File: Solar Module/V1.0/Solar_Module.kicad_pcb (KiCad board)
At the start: 2 copper layers, 4 parts, among them U1 MT3608, U2 TP4057

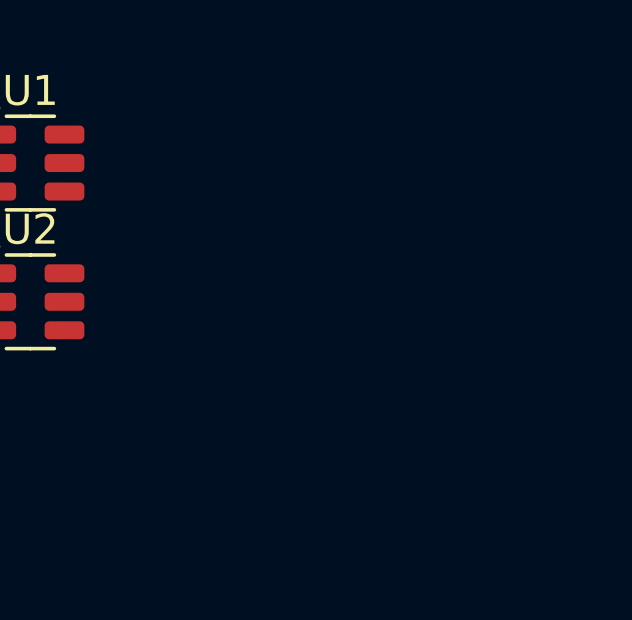
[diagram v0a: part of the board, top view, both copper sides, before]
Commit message: Added USB-C connector to schematic.
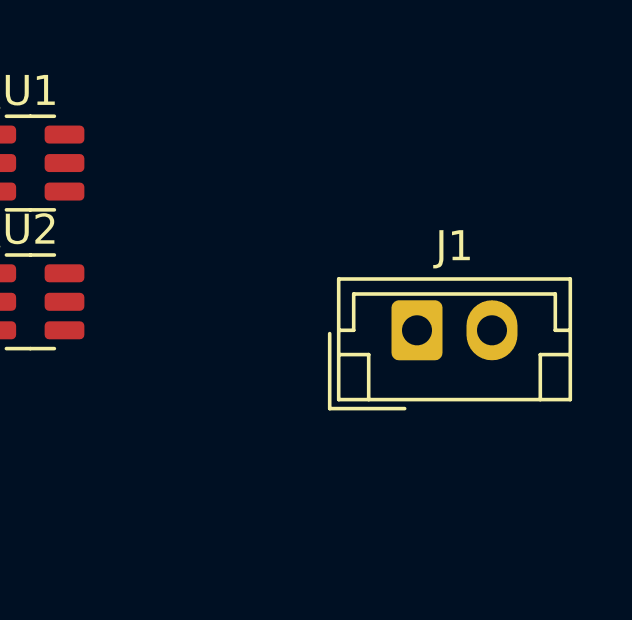
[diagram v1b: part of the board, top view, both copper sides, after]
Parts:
- added J1: B2B-PH-K-S, Connector_JST:JST_EH_B2B-EH-A_1x02_P2.50mm_Vertical, F.Cu at (99.8, 40.8)
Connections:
- U2 pad 1: unconnected-(U2-~{CHRG}-Pad1) -> /CHRG
- U2 pad 2: unconnected-(U2-GND-Pad2) -> GND
- U2 pad 3: unconnected-(U2-BAT-Pad3) -> /BAT_OUT
- U2 pad 4: unconnected-(U2-VCC-Pad4) -> +5V
- U2 pad 5: unconnected-(U2-~{STDBY}-Pad5) -> /STDBY
- U2 pad 6: unconnected-(U2-PROG-Pad6) -> /PROG

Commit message: Rough design of DCDC.
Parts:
- added C1: 22u/16V, Capacitor_SMD:C_0805_2012Metric, F.Cu at (173.0, 51.5)
- added C2: 22u/16V, Capacitor_SMD:C_0805_2012Metric, F.Cu at (173.0, 53.5)
- added C3: 10u/16V, Capacitor_SMD:C_0805_2012Metric, F.Cu at (68.5, 43.1)
- added C4: 10u/16V, Capacitor_SMD:C_0805_2012Metric, F.Cu at (68.5, 46.2)
- added D2: LED, LED_SMD:LED_0603_1608Metric, F.Cu at (68.3, 56.1)
- added D3: LED, LED_SMD:LED_0603_1608Metric, F.Cu at (68.3, 58.6)
- added F1: CFS06V3T1R0, Fuse:Fuse_0603_1608Metric, F.Cu at (64.3, 36.9)
- added J2: TYPE-C16PIN, Connector_USB:USB_C_Receptacle_GCT_USB4105-xx-A_16P_TopMnt_Horizontal, F.Cu at (121.4, 44.6)
- added J3: B2B-PH-K-S, Connector_JST:JST_EH_B2B-EH-A_1x02_P2.50mm_Vertical, F.Cu at (74.2, 44.1)
- added JP1: SolderJumper_2_Open, Jumper:SolderJumper-2_P1.3mm_Open_TrianglePad1.0x1.5mm, F.Cu at (165.2, 57.8)
- added JP2: SolderJumper_2_Open, Jumper:SolderJumper-2_P1.3mm_Open_TrianglePad1.0x1.5mm, F.Cu at (68.5, 53.0)
- added R1: 750k, Resistor_SMD:R_0603_1608Metric, F.Cu at (176.3, 53.5)
- added R2: 100k, Resistor_SMD:R_0603_1608Metric, F.Cu at (176.3, 51.5)
- added R3: 4k, Resistor_SMD:R_0603_1608Metric, F.Cu at (64.3, 44.4)
- added R4: 1k, Resistor_SMD:R_0603_1608Metric, F.Cu at (64.3, 46.9)
- added R6: 5k1, Resistor_SMD:R_0603_1608Metric, F.Cu at (64.3, 49.4)
- added R7: 5k1, Resistor_SMD:R_0603_1608Metric, F.Cu at (64.3, 51.9)
- added R8: 1M, Resistor_SMD:R_0603_1608Metric, F.Cu at (64.3, 54.5)
- moved D1 95.6 mm to (168.8, 50.0), turned to 90 degrees
- moved L1 95.3 mm to (171.9, 42.6), turned to 180 degrees
- moved U1 87.2 mm to (173.0, 48.8)
- moved J1 25.6 mm to (74.2, 38.2)
- moved U2 14.7 mm to (85.0, 54.4)
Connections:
- J1 pad 1: unconnected-(J1-Pin_1-Pad1) -> 3V_Solar
- J1 pad 2: unconnected-(J1-Pin_2-Pad2) -> GND
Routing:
- net /FB: track 0.00 -> 9.27 mm, vias 0 -> 2
- net /5V_Out: track 0.00 -> 7.16 mm
- added copper zone on F.Cu, net /5V_Out
- added copper zone on F.Cu, net /SW
- added copper zone on F.Cu, net 3V_Solar
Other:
- copper layers 2 -> 4

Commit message: Continued with layout of BMS IC.
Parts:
- moved JP2 87.6 mm to (144.0, 97.3)
- moved R3 75.1 mm to (128.1, 83.9), turned to -90 degrees
- moved C3 71.8 mm to (125.4, 87.0), turned to 180 degrees
- moved R4 71.2 mm to (127.1, 80.5), turned to 90 degrees
- moved C4 65.4 mm to (121.8, 84.1), turned to 90 degrees
- moved D3 61.2 mm to (125.5, 80.5), turned to 90 degrees
- moved J3 61.0 mm to (132.2, 63.2)
- moved D2 60.6 mm to (123.8, 80.5), turned to 90 degrees
- moved U2 49.9 mm to (125.1, 84.1)
- moved C1 3.13 mm to (172.6, 48.4)
- moved C2 3.13 mm to (172.6, 50.4)
- moved D1 3.13 mm to (168.4, 46.9)
- moved L1 3.13 mm to (171.5, 39.5)
- moved R1 3.13 mm to (175.9, 50.4)
- moved R2 3.13 mm to (175.9, 48.4)
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
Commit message: Progressed with Design. Now in a solid state.
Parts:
- moved F1 114.4 mm to (174.2, 68.5)
- moved R8 108.3 mm to (172.5, 59.0), turned to -90 degrees
- moved R6 107.2 mm to (171.0, 59.0), turned to 90 degrees
- moved R7 105.5 mm to (169.5, 59.0), turned to -90 degrees
- moved J1 87.4 mm to (155.2, 71.0)
- moved J2 62.5 mm to (181.2, 62.5)
- moved C4 53.0 mm to (170.4, 62.8), turned to 0 degrees
- moved D2 52.6 mm to (174.2, 65.5), turned to 0 degrees
- moved D3 50.6 mm to (174.3, 67.0), turned to 0 degrees
- moved R4 50.5 mm to (174.2, 62.5), turned to 0 degrees
- moved R3 50.3 mm to (174.2, 64.0), turned to 0 degrees
- moved U2 48.8 mm to (170.4, 66.0), turned to -90 degrees
- moved C3 46.8 mm to (167.5, 66.4), turned to 90 degrees
- moved JP2 37.7 mm to (171.0, 70.9), turned to -90 degrees
- moved J3 32.8 mm to (164.0, 71.0)
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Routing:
- net /FB: track 9.27 -> 0.00 mm, vias 2 -> 0
- net /5V_Out: track 7.16 -> 0.00 mm
- removed copper zone on F.Cu, net /5V_Out
- removed copper zone on F.Cu, net /SW
- removed copper zone on F.Cu, net 3V_Solar
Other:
- board text added: "5V"
- board text added: "BATT"

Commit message: Design roughly finished. Now Routing.
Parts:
- moved C3 1.12 mm to (168.0, 65.4)
- moved C4 1.12 mm to (170.9, 61.8)
- moved D2 1.12 mm to (174.8, 64.5)
- moved D3 1.12 mm to (174.8, 66.0)
- moved F1 1.12 mm to (174.8, 67.5)
- moved R3 1.12 mm to (174.8, 63.0)
- moved R4 1.12 mm to (174.8, 61.5)
- moved U2 1.12 mm to (170.9, 65.0)
- moved J2 0.64 mm to (181.9, 62.5)
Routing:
- net /VBUS_OUT: track 0.00 -> 6.59 mm
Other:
- board outline added: 34.2 x 19.5 mm
- board text added: "Akku"
- board text added: "OUT"
- board text added: "Solar Panel"
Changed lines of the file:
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@@
 	(footprint "LED_SMD:LED_0603_1608Metric"
 		(layer "F.Cu")
-		(at 174.250002 66.999999)
+		(at 174.750002 66)
 		(descr "LED SMD 0603 (1608 Metric), square (rectangular) end terminal, IPC_7351 nominal, (Body size source: http://www.tortai-tech.com/upload/download/2011102023233369053.pdf), generated with kicad-footprint-generator")
 		(tags "LED")
@@
 	(footprint "LED_SMD:LED_0603_1608Metric"
 		(layer "F.Cu")
-		(at 174.25 65.499999)
+		(at 174.75 64.5)
 		(descr "LED SMD 0603 (1608 Metric), square (rectangular) end terminal, IPC_7351 nominal, (Body size source: http://www.tortai-tech.com/upload/download/2011102023233369053.pdf), generated with kicad-footprint-generator")
 		(tags "LED")
@@
 	(footprint "Resistor_SMD:R_0603_1608Metric"
 		(layer "F.Cu")
-		(at 174.25 62.5)
+		(at 174.75 61.500001)
 		(descr "Resistor SMD 0603 (1608 Metric), square (rectangular) end terminal, IPC_7351 nominal, (Body size source: IPC-SM-782 page 72, https://www.pcb-3d.com/wordpress/wp-content/uploads/ipc-sm-782a_amendment_1_and_2.pdf), generated with kicad-footprint-generator")
 		(tags "resistor")
@@
 	(footprint "Capacitor_SMD:C_0805_2012Metric"
 		(layer "F.Cu")
-		(at 170.375002 62.799998)
+		(at 170.875002 61.799999)
 		(descr "Capacitor SMD 0805 (2012 Metric), square (rectangular) end terminal, IPC_7351 nominal, (Body size source: IPC-SM-782 page 76, https://www.pcb-3d.com/wordpress/wp-content/uploads/ipc-sm-782a_amendment_1_and_2.pdf, https://docs.google.com/spreadsheets/d/1BsfQQcO9C6DZCsRaXUlFlo91Tg2WpOkGARC1WS5S8t0/edit?usp=sharing), generated with kicad-footprint-generator")
 		(tags "capacitor")
@@
 	(footprint "Resistor_SMD:R_0603_1608Metric"
 		(layer "F.Cu")
-		(at 174.25 64)
+		(at 174.75 63.000001)
 		(descr "Resistor SMD 0603 (1608 Metric), square (rectangular) end terminal, IPC_7351 nominal, (Body size source: IPC-SM-782 page 72, https://www.pcb-3d.com/wordpress/wp-content/uploads/ipc-sm-782a_amendment_1_and_2.pdf), generated with kicad-footprint-generator")
 		(tags "resistor")
@@
 	(footprint "Package_TO_SOT_SMD:SOT-23-6"
 		(layer "F.Cu")
-		(at 170.375002 65.999998 -90)
+		(at 170.875002 64.999999 -90)
 		(descr "SOT, 6 Pin (https://www.jedec.org/sites/default/files/docs/Mo-178c.PDF variant AB), generated with kicad-footprint-generator ipc_gullwing_generator.py")
 		(tags "SOT TO_SOT_SMD")
@@
 	(footprint "Connector_USB:USB_C_Receptacle_GCT_USB4105-xx-A_16P_TopMnt_Horizontal"
 		(layer "F.Cu")
-		(at 181.25 62.5 90)
+		(at 181.89 62.5 90)
 		(descr "USB 2.0 Type C Receptacle, GCT, 16P, top mounted, horizontal, 5A: https://gct.co/files/drawings/usb4105.pdf")
 		(tags "USB C Type-C Receptacle SMD USB 2.0 16P 16C USB4105-15-A USB4105-15-A-060 USB4105-15-A-120 USB4105-GF-A USB4105-GF-A-060 USB4105-GF-A-120")
@@
 	(footprint "Fuse:Fuse_0603_1608Metric"
 		(layer "F.Cu")
-		(at 174.25 68.5)
+		(at 174.75 67.500001)
 		(descr "Fuse SMD 0603 (1608 Metric), square (rectangular) end terminal, IPC_7351 nominal, (Body size source: http://www.tortai-tech.com/upload/download/2011102023233369053.pdf), generated with kicad-footprint-generator")
 		(tags "fuse")
@@
 	(footprint "Capacitor_SMD:C_0805_2012Metric"
 		(layer "F.Cu")
-		(at 167.475002 66.399998 90)
+		(at 167.975002 65.399999 90)
 		(descr "Capacitor SMD 0805 (2012 Metric), square (rectangular) end terminal, IPC_7351 nominal, (Body size source: IPC-SM-782 page 76, https://www.pcb-3d.com/wordpress/wp-content/uploads/ipc-sm-782a_amendment_1_and_2.pdf, https://docs.google.com/spreadsheets/d/1BsfQQcO9C6DZCsRaXUlFlo91Tg2WpOkGARC1WS5S8t0/edit?usp=sharing), generated with kicad-footprint-generator")
 		(tags "capacitor")
@@
 		)
 	)
+	(gr_line
+		(start 185.6 76)
+		(end 185.6 56.5)
+		(stroke
+			(width 0.05)
+			(type default)
+		)
+		(layer "Edge.Cuts")
+	)
+	(gr_line
+		(start 151.4 56.5)
+		(end 151.4 76)
+		(stroke
+			(width 0.05)
+			(type default)
+		)
+		(layer "Edge.Cuts")
+	)
+	(gr_line
+		(start 151.4 76)
+		(end 185.6 76)
+		(stroke
+			(width 0.05)
+			(type default)
+		)
+		(layer "Edge.Cuts")
+	)
+	(gr_line
+		(start 185.6 56.5)
+		(end 151.4 56.5)
+		(stroke
+			(width 0.05)
+			(type default)
+		)
+		(layer "Edge.Cuts")
+	)
 	(gr_text "5V"
-		(at 165.2 64.6 0)
+		(at 165.25 64.6 0)
+		(layer "F.SilkS" knockout)
+		(effects
+			(font
+				(size 0.8 0.8)
+				(thickness 0.15)
+				(bold yes)
+			)
+			(justify left bottom)
+		)
+	)
+	(gr_text "Akku"
+		(at 161 75 0)
 		(layer "F.SilkS" knockout)
 		(effects
@@
 		)
 	)
+	(gr_text "Solar Panel"
+		(at 152.25 75 0)
+		(layer "F.SilkS" knockout)
+		(effects
+			(font
+				(size 0.8 0.8)
+				(thickness 0.15)
+				(bold yes)
+			)
+			(justify left bottom)
+		)
+	)
+	(gr_text "OUT"
+		(at 177.25 69.25 0)
+		(layer "F.SilkS" knockout)
+		(effects
+			(font
+				(size 0.8 0.8)
+				(thickness 0.15)
+				(bold yes)
+			)
+			(justify left bottom)
+		)
+	)
+	(segment
+		(start 178.21 60.1)
+		(end 177.540458 60.1)
+		(width 0.5)
+		(layer "F.Cu")
+		(net 14)
+	)
+	(segment
+		(start 177 64.359542)
+		(end 177.540458 64.9)
+		(width 0.5)
+		(layer "F.Cu")
+		(net 14)
+	)
+	(segment
+		(start 177.540458 60.1)
+		(end 177 60.640458)
+		(width 0.5)
+		(layer "F.Cu")
+		(net 14)
+	)
+	(segment
+		(start 177 60.640458)
+		(end 177 64.359542)
+		(width 0.5)
+		(layer "F.Cu")
+		(net 14)
+	)
+	(segment
+		(start 177.540458 64.9)
+		(end 178.21 64.9)
+		(width 0.5)
+		(layer "F.Cu")
+		(net 14)
+	)
 )

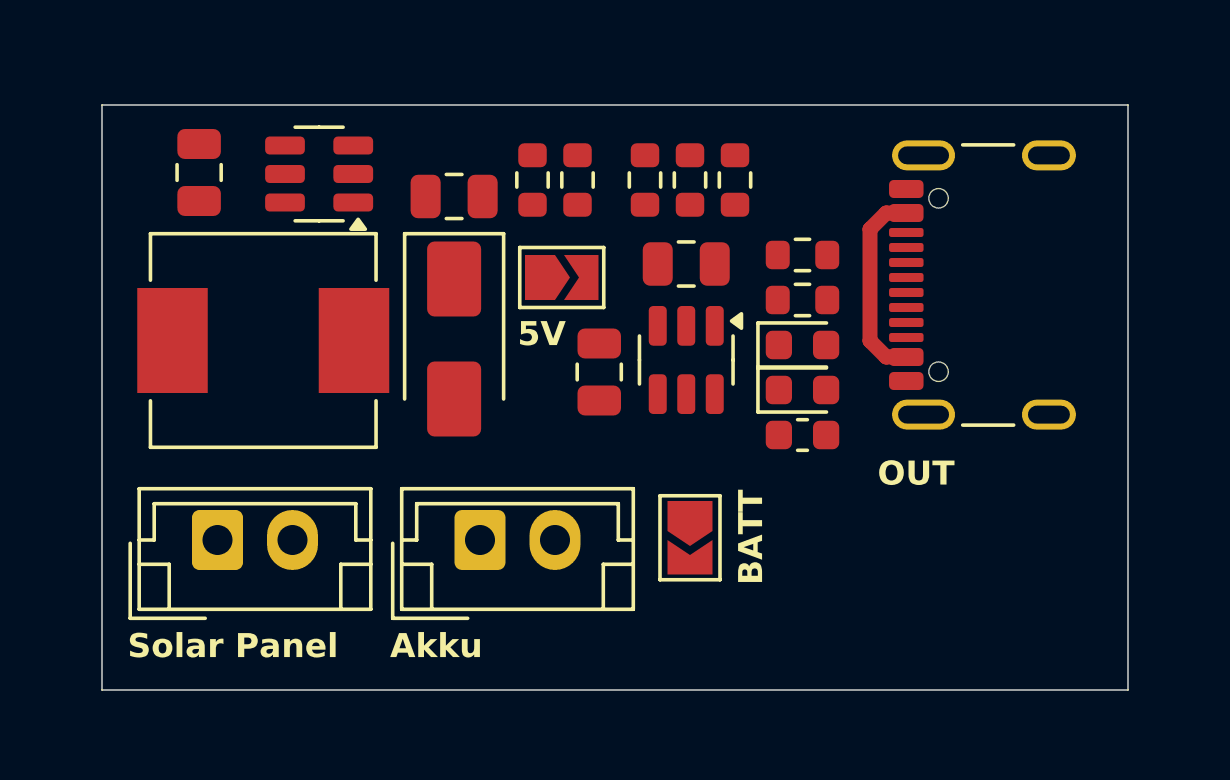
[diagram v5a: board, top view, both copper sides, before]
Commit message: V1 Design nearly finished. Only Edges needed to be round.
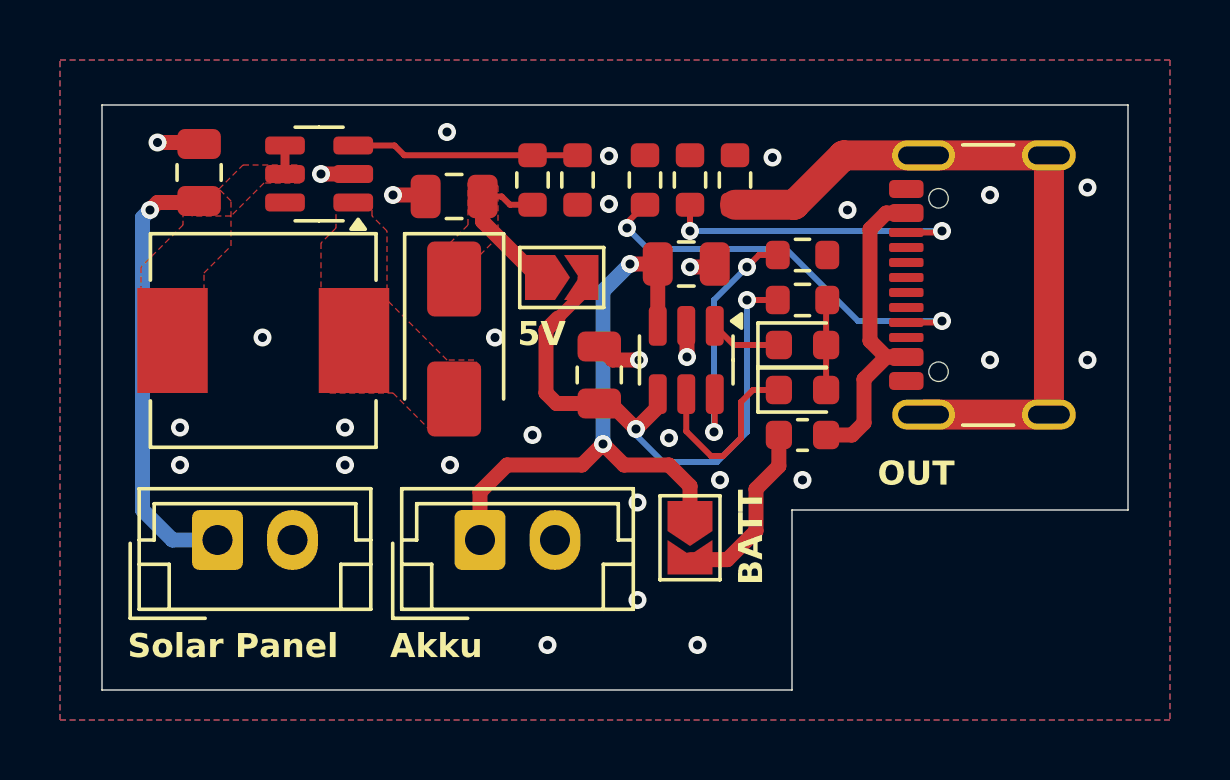
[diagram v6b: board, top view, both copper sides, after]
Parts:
- moved R3 1.50 mm to (174.8, 61.5)
- moved R4 1.50 mm to (174.8, 63.0)
- moved C3 0.10 mm to (168.0, 65.5)
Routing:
- net /Shield: track 0.00 -> 24.0 mm
- net /BAT_OUT: track 0.00 -> 20.2 mm, vias 0 -> 2
- net +5V: track 0.00 -> 19.4 mm, vias 0 -> 2
- net 3V_Solar: track 0.00 -> 15.7 mm, vias 0 -> 1
- net /CC1: track 0.00 -> 14.0 mm, vias 0 -> 2
- net /CC2: track 0.00 -> 10.5 mm, vias 0 -> 2
- net /PROG: track 0.00 -> 8.42 mm, vias 0 -> 2
- net /FB: track 0.00 -> 7.61 mm
- net GND: track 0.00 -> 7.02 mm, vias 0 -> 30
- net /STDBY: track 0.00 -> 6.28 mm
- net VBUS: track 0.00 -> 6.11 mm
- net /5V_Out: track 0.00 -> 5.30 mm
- net /VBUS_OUT: track 6.59 -> 10.5 mm
- net Net-(D2-A): track 0.00 -> 3.02 mm
- net /CHRG: track 0.00 -> 2.40 mm
- added copper zone on F.Cu, net /5V_Out
- added copper zone on F.Cu, net /SW
- added copper zone on F.Cu, net 3V_Solar
- added copper zone on B.Cu, net GND
- added copper zone on F.Cu, net GND
- added copper zone on In1.Cu, net GND
- added copper zone on In2.Cu, net GND
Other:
- outline, holes or cut-outs redrawn
